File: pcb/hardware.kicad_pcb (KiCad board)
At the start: 2 copper layers, 16 parts, among them J1 Micro_SD_Card_Det_Hirose_DM3AT, U1 AS4C512M16D3L-12BIN, U2 A33, U3 TPS62095RGTR

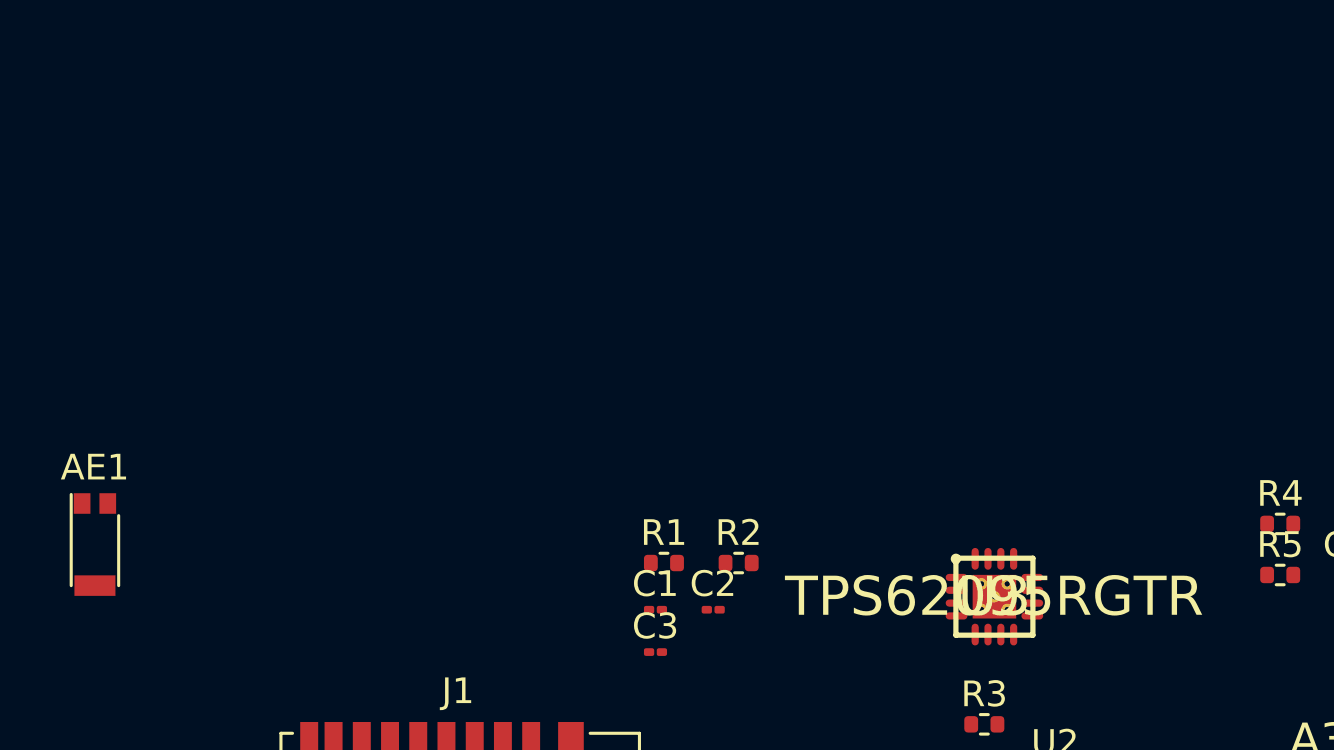
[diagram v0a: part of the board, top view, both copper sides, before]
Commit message: Added the 2.5V LDO
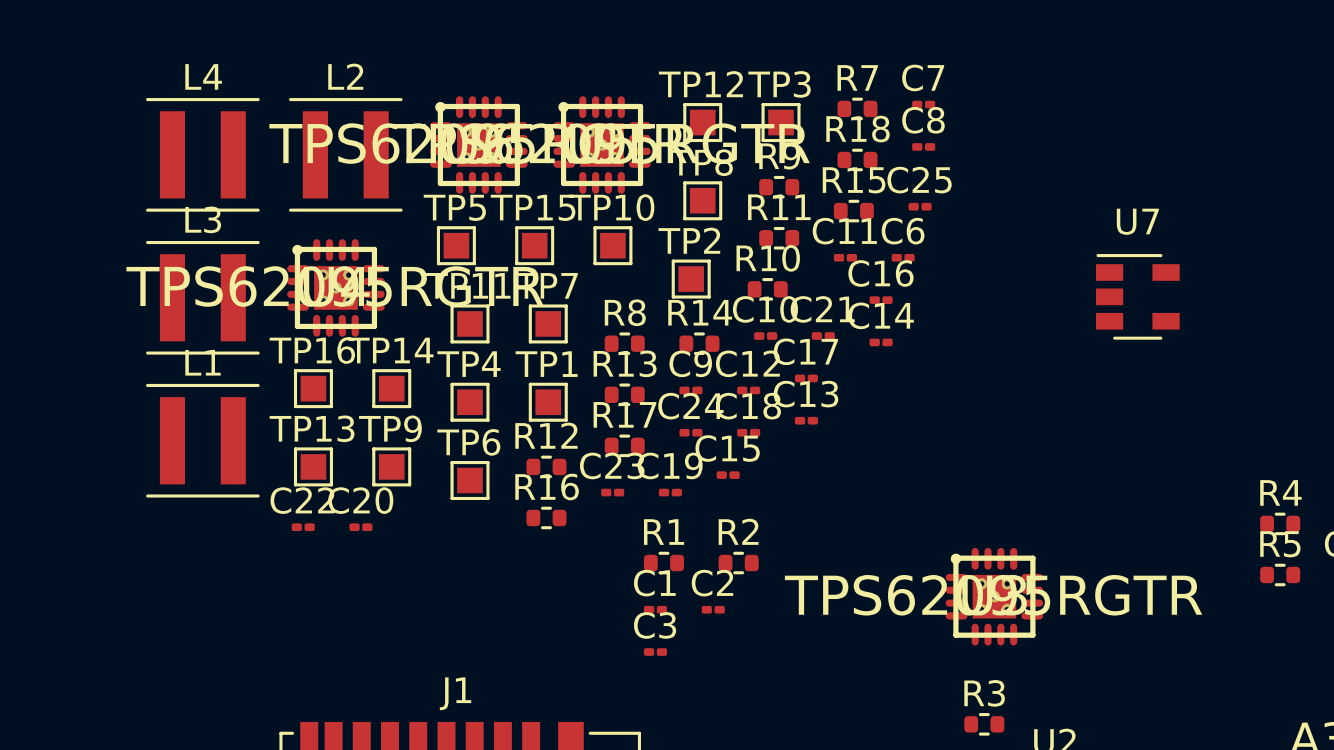
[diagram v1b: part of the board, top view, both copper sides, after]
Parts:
- removed AE1: Antenna, RF_Antenna:Pulse_W3011
- added C10: 22uF, Capacitor_SMD:C_01005_0402Metric, F.Cu at (120.1, 78.7)
- added C11: 22uF, Capacitor_SMD:C_01005_0402Metric, F.Cu at (123.2, 75.7)
- added C12: 10nF, Capacitor_SMD:C_01005_0402Metric, F.Cu at (119.5, 80.9)
- added C13: 450pF, Capacitor_SMD:C_01005_0402Metric, F.Cu at (121.7, 82.0)
- added C14: 22uF, Capacitor_SMD:C_01005_0402Metric, F.Cu at (124.6, 79.0)
- added C15: 22uF, Capacitor_SMD:C_01005_0402Metric, F.Cu at (118.7, 84.2)
- added C16: 22uF, Capacitor_SMD:C_01005_0402Metric, F.Cu at (124.6, 77.3)
- added C17: 22uF, Capacitor_SMD:C_01005_0402Metric, F.Cu at (121.7, 80.4)
- added C18: 10nF, Capacitor_SMD:C_01005_0402Metric, F.Cu at (119.5, 82.5)
- added C19: 5nF, Capacitor_SMD:C_01005_0402Metric, F.Cu at (116.4, 84.8)
- added C20: 10nF, Capacitor_SMD:C_01005_0402Metric, F.Cu at (104.3, 86.2)
- added C21: 5nF, Capacitor_SMD:C_01005_0402Metric, F.Cu at (122.4, 78.7)
- added C22: 22uF, Capacitor_SMD:C_01005_0402Metric, F.Cu at (102.1, 86.2)
- added C23: 22uF, Capacitor_SMD:C_01005_0402Metric, F.Cu at (114.2, 84.8)
- added C24: 22uF, Capacitor_SMD:C_01005_0402Metric, F.Cu at (117.2, 82.5)
- added C25: 22uF, Capacitor_SMD:C_01005_0402Metric, F.Cu at (126.1, 73.7)
- added C6: 22uF, Capacitor_SMD:C_01005_0402Metric, F.Cu at (125.5, 75.7)
- added C7: 10nF, Capacitor_SMD:C_01005_0402Metric, F.Cu at (126.3, 69.7)
- added C8: 450pF, Capacitor_SMD:C_01005_0402Metric, F.Cu at (126.3, 71.4)
- added C9: 22uF, Capacitor_SMD:C_01005_0402Metric, F.Cu at (117.2, 80.9)
- added L1: 1uH, Inductor_SMD:L_Coilcraft_XxL4020, F.Cu at (98.2, 82.8)
- added L2: 1uH, Inductor_SMD:L_Coilcraft_XxL4020, F.Cu at (103.8, 71.7)
- added L3: 1uH, Inductor_SMD:L_Coilcraft_XxL4020, F.Cu at (98.2, 77.3)
- added L4: 1uH, Inductor_SMD:L_Coilcraft_XxL4020, F.Cu at (98.2, 71.7)
- added R10: 120k, Resistor_SMD:R_0402_1005Metric, F.Cu at (120.2, 76.9)
- added R11: 110k, Resistor_SMD:R_0402_1005Metric, F.Cu at (120.6, 74.9)
- added R12: 160k, Resistor_SMD:R_0402_1005Metric, F.Cu at (111.6, 83.8)
- added R13: 82k, Resistor_SMD:R_0402_1005Metric, F.Cu at (114.6, 81.0)
- added R14: 220k, Resistor_SMD:R_0402_1005Metric, F.Cu at (117.5, 79.0)
- added R15: 0R, Resistor_SMD:R_0402_1005Metric, F.Cu at (123.6, 73.9)
- added R16: 0R, Resistor_SMD:R_0402_1005Metric, F.Cu at (111.6, 85.8)
- added R17: 0R, Resistor_SMD:R_0402_1005Metric, F.Cu at (114.6, 83.0)
- added R18: 0R, Resistor_SMD:R_0402_1005Metric, F.Cu at (123.7, 71.9)
- added R7: 470k, Resistor_SMD:R_0402_1005Metric, F.Cu at (123.7, 69.9)
- added R8: 150k, Resistor_SMD:R_0402_1005Metric, F.Cu at (114.6, 79.0)
- added R9: 330k, Resistor_SMD:R_0402_1005Metric, F.Cu at (120.6, 72.9)
- added TP1: TestPoint, TestPoint:TestPoint_Pad_1.0x1.0mm, F.Cu at (111.6, 81.3)
- added TP10: TestPoint, TestPoint:TestPoint_Pad_1.0x1.0mm, F.Cu at (114.2, 75.2)
- added TP11: TestPoint, TestPoint:TestPoint_Pad_1.0x1.0mm, F.Cu at (108.6, 78.3)
- added TP12: TestPoint, TestPoint:TestPoint_Pad_1.0x1.0mm, F.Cu at (117.7, 70.4)
- added TP13: TestPoint, TestPoint:TestPoint_Pad_1.0x1.0mm, F.Cu at (102.5, 83.8)
- added TP14: TestPoint, TestPoint:TestPoint_Pad_1.0x1.0mm, F.Cu at (105.5, 80.8)
- added TP15: TestPoint, TestPoint:TestPoint_Pad_1.0x1.0mm, F.Cu at (111.1, 75.2)
- added TP16: TestPoint, TestPoint:TestPoint_Pad_1.0x1.0mm, F.Cu at (102.5, 80.8)
- added TP2: TestPoint, TestPoint:TestPoint_Pad_1.0x1.0mm, F.Cu at (117.2, 76.5)
- added TP3: TestPoint, TestPoint:TestPoint_Pad_1.0x1.0mm, F.Cu at (120.7, 70.4)
- added TP4: TestPoint, TestPoint:TestPoint_Pad_1.0x1.0mm, F.Cu at (108.6, 81.3)
- added TP5: TestPoint, TestPoint:TestPoint_Pad_1.0x1.0mm, F.Cu at (108.1, 75.2)
- added TP6: TestPoint, TestPoint:TestPoint_Pad_1.0x1.0mm, F.Cu at (108.6, 84.4)
- added TP7: TestPoint, TestPoint:TestPoint_Pad_1.0x1.0mm, F.Cu at (111.6, 78.3)
- added TP8: TestPoint, TestPoint:TestPoint_Pad_1.0x1.0mm, F.Cu at (117.7, 73.5)
- added TP9: TestPoint, TestPoint:TestPoint_Pad_1.0x1.0mm, F.Cu at (105.5, 83.8)
- added U4: TPS62095RGTR, TI:TI_RTE_S-PWQFN-N16, F.Cu at (103.4, 76.9)
- added U5: TPS62095RGTR, TI:TI_RTE_S-PWQFN-N16, F.Cu at (113.7, 71.3)
- added U6: TPS62095RGTR, TI:TI_RTE_S-PWQFN-N16, F.Cu at (108.9, 71.3)
- added U7: AP131-25, Package_TO_SOT_SMD:SOT-23-5, F.Cu at (134.6, 77.2)
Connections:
- U2 pad K1: Net-(U2-PadK1) -> /ram/!LDQS
- U2 pad K2: Net-(U2-PadK2) -> /ram/LDQS
- U2 pad L12: +3V0 -> +3V3
- U2 pad N2: Net-(U2-PadN2) -> /ram/LDM
- U2 pad R1: Net-(U2-PadR1) -> /ram/!UDQS
- U2 pad T1: Net-(U2-PadT1) -> /ram/UDQS
- U2 pad T3: Net-(U2-PadT3) -> /ram/UDM
- U3 pad 1: Net-(U3-Pad1) -> Net-(L1-Pad1)
- U3 pad 10: Net-(U3-Pad10) -> +5V
- U3 pad 11: Net-(U3-Pad11) -> +5V
- U3 pad 12: Net-(U3-Pad12) -> +5V
- U3 pad 13: Net-(U3-Pad13) -> +5V
- U3 pad 14: Net-(U3-Pad14) -> GND
- U3 pad 15: Net-(U3-Pad15) -> GND
- U3 pad 17: Net-(U3-Pad17) -> GND
- U3 pad 2: Net-(U3-Pad2) -> Net-(L1-Pad1)
- U3 pad 3: Net-(U3-Pad3) -> +5V
- U3 pad 6: Net-(U3-Pad6) -> GND

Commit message: Random unknown commit
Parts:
- added C26: 10uF, Capacitor_SMD:C_01005_0402Metric, F.Cu at (179.1, 47.0)
- added C27: 0.1uF, Capacitor_SMD:C_01005_0402Metric, F.Cu at (182.3, 43.9)
- added C28: 10uF, Capacitor_SMD:C_01005_0402Metric, F.Cu at (181.3, 47.0)
- added R19: 0R, Resistor_SMD:R_0402_1005Metric, F.Cu at (176.5, 47.2)
- added R20: 100k, Resistor_SMD:R_0402_1005Metric, F.Cu at (148.2, 84.8)
- added R21: 100k, Resistor_SMD:R_0402_1005Metric, F.Cu at (151.1, 84.8)
- added R22: 10k, Resistor_SMD:R_0402_1005Metric, F.Cu at (154.0, 84.8)
- added R23: 100k, Resistor_SMD:R_0402_1005Metric, F.Cu at (148.2, 86.7)
- added R24: 100k, Resistor_SMD:R_0402_1005Metric, F.Cu at (151.1, 86.7)
- added R25: 100k, Resistor_SMD:R_0402_1005Metric, F.Cu at (148.2, 88.7)
- added TP17: TestPoint, TestPoint:TestPoint_Pad_1.0x1.0mm, F.Cu at (176.6, 44.6)
- added TP18: TestPoint, TestPoint:TestPoint_Pad_1.0x1.0mm, F.Cu at (179.6, 44.6)
- moved R4 52.6 mm to (88.1, 93.7)
- moved R5 52.6 mm to (88.1, 95.7)
- moved R6 52.6 mm to (91.0, 93.7)
- moved C4 52.6 mm to (90.7, 95.5)
- moved C5 52.6 mm to (92.9, 95.5)
- moved U3 49.6 mm to (79.5, 91.4)
- moved R3 49.6 mm to (79.1, 96.4)
- moved J1 32.5 mm to (135.9, 85.1), turned to 180 degrees
- moved C10 25.5 mm to (94.7, 76.2)
- moved C11 25.5 mm to (97.8, 73.2)
- moved C12 25.5 mm to (94.1, 78.3)
- moved C13 25.5 mm to (96.3, 79.5)
- moved C14 25.5 mm to (99.2, 76.5)
- moved C15 25.5 mm to (93.3, 81.6)
- moved C16 25.5 mm to (99.2, 74.8)
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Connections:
- J1 pad 1: Net-(J1-Pad1) -> /gpio/SD_DAT2
- J1 pad 10: Net-(J1-Pad10) -> /gpio/SD_DET
- J1 pad 11: Net-(J1-Pad11) -> GND
- J1 pad 2: Net-(J1-Pad2) -> /gpio/SD_DAT3
- J1 pad 3: Net-(J1-Pad3) -> /gpio/SD_CMD
- J1 pad 4: Net-(J1-Pad4) -> +3V3
- J1 pad 5: Net-(J1-Pad5) -> /gpio/SD_CLK
- J1 pad 6: Net-(J1-Pad6) -> GND
- J1 pad 7: Net-(J1-Pad7) -> /gpio/SD_DAT0
- J1 pad 8: Net-(J1-Pad8) -> /gpio/SD_DAT1
- J1 pad 9: Net-(J1-Pad9) -> GND
- U2 pad C7: Net-(U2-PadC7) -> /gpio/SD_DAT2
- U2 pad C8: Net-(U2-PadC8) -> /gpio/SD_CMD
- U2 pad C9: Net-(U2-PadC9) -> /gpio/SD_DAT0
- U2 pad D7: Net-(U2-PadD7) -> /gpio/SD_DAT3
- U2 pad D8: Net-(U2-PadD8) -> /gpio/SD_CLK
- U2 pad D9: Net-(U2-PadD9) -> /gpio/SD_DAT1
- U2 pad G14: Net-(U2-PadG14) -> /gpio/SD_DET
- U7 pad 1: Net-(U7-Pad1) -> +3V3
- U7 pad 2: Net-(U7-Pad2) -> GND
- U7 pad 3: Net-(U7-Pad3) -> +3V3

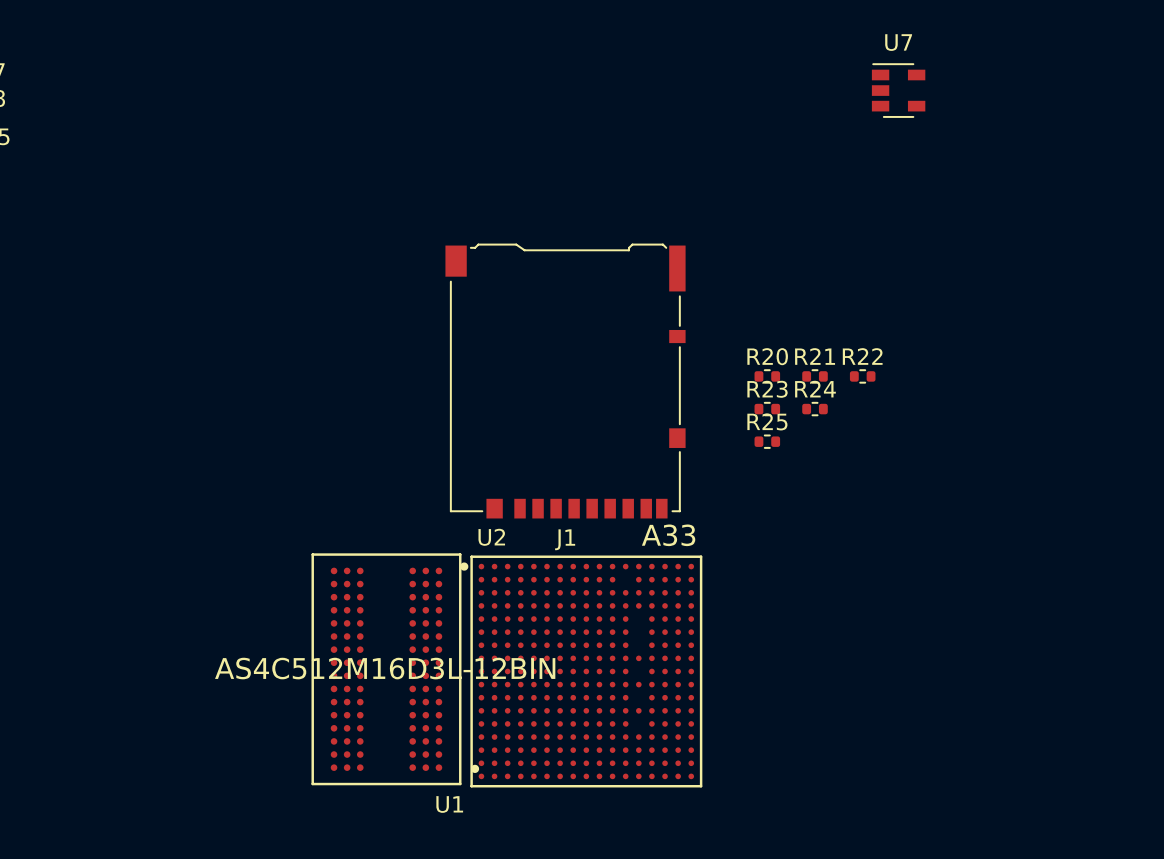
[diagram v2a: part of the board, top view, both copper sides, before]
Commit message: Just dropped all the parts on the board.
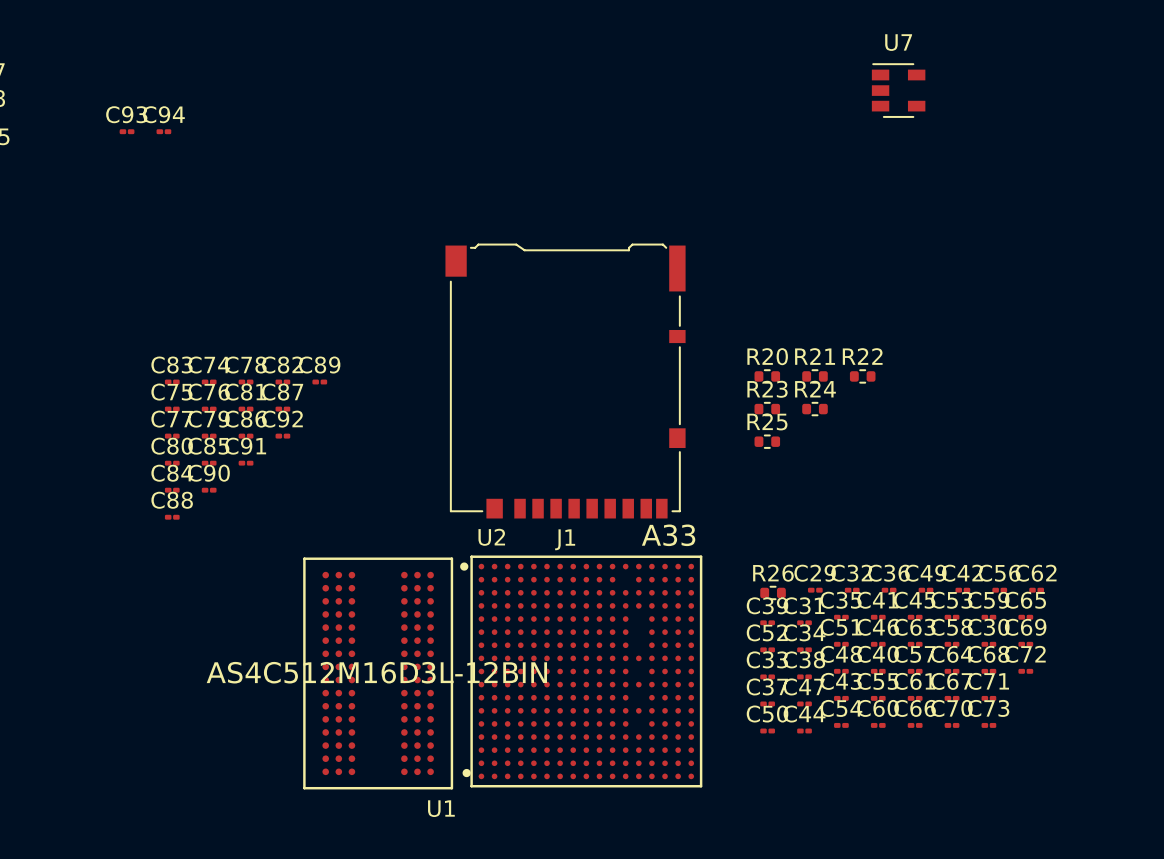
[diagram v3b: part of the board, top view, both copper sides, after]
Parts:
- added C29: 10uF, Capacitor_SMD:C_01005_0402Metric, F.Cu at (151.1, 97.8)
- added C30: 100nF, Capacitor_SMD:C_01005_0402Metric, F.Cu at (161.7, 101.1)
- added C31: 100nF, Capacitor_SMD:C_01005_0402Metric, F.Cu at (150.5, 99.8)
- added C32: 100nF, Capacitor_SMD:C_01005_0402Metric, F.Cu at (153.4, 97.8)
- added C33: 100nF, Capacitor_SMD:C_01005_0402Metric, F.Cu at (148.2, 103.1)
- added C34: 100nF, Capacitor_SMD:C_01005_0402Metric, F.Cu at (150.5, 101.4)
- added C35: 100nF, Capacitor_SMD:C_01005_0402Metric, F.Cu at (152.7, 99.4)
- added C36: 100nF, Capacitor_SMD:C_01005_0402Metric, F.Cu at (155.6, 97.8)
- added C37: 100nF, Capacitor_SMD:C_01005_0402Metric, F.Cu at (148.2, 104.7)
- added C38: 100nF, Capacitor_SMD:C_01005_0402Metric, F.Cu at (150.5, 103.1)
- added C39: 100nF, Capacitor_SMD:C_01005_0402Metric, F.Cu at (148.2, 99.8)
- added C40: 100nF, Capacitor_SMD:C_01005_0402Metric, F.Cu at (155.0, 102.7)
- added C41: 100nF, Capacitor_SMD:C_01005_0402Metric, F.Cu at (155.0, 99.4)
- added C42: 100nF, Capacitor_SMD:C_01005_0402Metric, F.Cu at (160.1, 97.8)
- added C43: 100nF, Capacitor_SMD:C_01005_0402Metric, F.Cu at (152.7, 104.4)
- added C44: 100nF, Capacitor_SMD:C_01005_0402Metric, F.Cu at (150.5, 106.4)
- added C45: 100nF, Capacitor_SMD:C_01005_0402Metric, F.Cu at (157.2, 99.4)
- added C46: 100nF, Capacitor_SMD:C_01005_0402Metric, F.Cu at (155.0, 101.1)
- added C47: 100nF, Capacitor_SMD:C_01005_0402Metric, F.Cu at (150.5, 104.7)
- added C48: 100nF, Capacitor_SMD:C_01005_0402Metric, F.Cu at (152.7, 102.7)
- added C49: 100nF, Capacitor_SMD:C_01005_0402Metric, F.Cu at (157.9, 97.8)
- added C50: 100nF, Capacitor_SMD:C_01005_0402Metric, F.Cu at (148.2, 106.4)
- added C51: 100nF, Capacitor_SMD:C_01005_0402Metric, F.Cu at (152.7, 101.1)
- added C52: 100nF, Capacitor_SMD:C_01005_0402Metric, F.Cu at (148.2, 101.4)
- added C53: 22uF, Capacitor_SMD:C_01005_0402Metric, F.Cu at (159.5, 99.4)
- added C54: 22uF, Capacitor_SMD:C_01005_0402Metric, F.Cu at (152.7, 106.0)
- added C55: 100nF, Capacitor_SMD:C_01005_0402Metric, F.Cu at (155.0, 104.4)
- added C56: 100nF, Capacitor_SMD:C_01005_0402Metric, F.Cu at (162.4, 97.8)
- added C57: 22uF, Capacitor_SMD:C_01005_0402Metric, F.Cu at (157.2, 102.7)
- added C58: 22uF, Capacitor_SMD:C_01005_0402Metric, F.Cu at (159.5, 101.1)
- added C59: 100nF, Capacitor_SMD:C_01005_0402Metric, F.Cu at (161.7, 99.4)
- added C60: 100nF, Capacitor_SMD:C_01005_0402Metric, F.Cu at (155.0, 106.0)
- added C61: 100nF, Capacitor_SMD:C_01005_0402Metric, F.Cu at (157.2, 104.4)
- added C62: 100nF, Capacitor_SMD:C_01005_0402Metric, F.Cu at (164.6, 97.8)
- added C63: 100nF, Capacitor_SMD:C_01005_0402Metric, F.Cu at (157.2, 101.1)
- added C64: 100nF, Capacitor_SMD:C_01005_0402Metric, F.Cu at (159.5, 102.7)
- added C65: 100nF, Capacitor_SMD:C_01005_0402Metric, F.Cu at (164.0, 99.4)
- added C66: 100nF, Capacitor_SMD:C_01005_0402Metric, F.Cu at (157.2, 106.0)
- added C67: 100nF, Capacitor_SMD:C_01005_0402Metric, F.Cu at (159.5, 104.4)
- added C68: 100nF, Capacitor_SMD:C_01005_0402Metric, F.Cu at (161.7, 102.7)
- added C69: 100nF, Capacitor_SMD:C_01005_0402Metric, F.Cu at (164.0, 101.1)
- added C70: 100nF, Capacitor_SMD:C_01005_0402Metric, F.Cu at (159.5, 106.0)
- added C71: 22uF, Capacitor_SMD:C_01005_0402Metric, F.Cu at (161.7, 104.4)
- added C72: 22uF, Capacitor_SMD:C_01005_0402Metric, F.Cu at (164.0, 102.7)
- added C73: 100nF, Capacitor_SMD:C_01005_0402Metric, F.Cu at (161.7, 106.0)
- added C74: 100nF, Capacitor_SMD:C_01005_0402Metric, F.Cu at (114.2, 85.1)
- added C75: 100nF, Capacitor_SMD:C_01005_0402Metric, F.Cu at (111.9, 86.7)
- added C76: 100nF, Capacitor_SMD:C_01005_0402Metric, F.Cu at (114.2, 86.7)
- added C77: 100nF, Capacitor_SMD:C_01005_0402Metric, F.Cu at (111.9, 88.4)
- added C78: 100nF, Capacitor_SMD:C_01005_0402Metric, F.Cu at (116.4, 85.1)
- added C79: 100nF, Capacitor_SMD:C_01005_0402Metric, F.Cu at (114.2, 88.4)
- added C80: 100nF, Capacitor_SMD:C_01005_0402Metric, F.Cu at (111.9, 90.0)
- added C81: 100nF, Capacitor_SMD:C_01005_0402Metric, F.Cu at (116.4, 86.7)
- added C82: 100nF, Capacitor_SMD:C_01005_0402Metric, F.Cu at (118.7, 85.1)
- added C83: 100nF, Capacitor_SMD:C_01005_0402Metric, F.Cu at (111.9, 85.1)
- added C84: 100nF, Capacitor_SMD:C_01005_0402Metric, F.Cu at (111.9, 91.7)
- added C85: 100nF, Capacitor_SMD:C_01005_0402Metric, F.Cu at (114.2, 90.0)
- added C86: 100nF, Capacitor_SMD:C_01005_0402Metric, F.Cu at (116.4, 88.4)
- added C87: 100nF, Capacitor_SMD:C_01005_0402Metric, F.Cu at (118.7, 86.7)
- added C88: 100nF, Capacitor_SMD:C_01005_0402Metric, F.Cu at (111.9, 93.3)
- added C89: 100nF, Capacitor_SMD:C_01005_0402Metric, F.Cu at (120.9, 85.1)
- added C90: 100nF, Capacitor_SMD:C_01005_0402Metric, F.Cu at (114.2, 91.7)
- added C91: 100nF, Capacitor_SMD:C_01005_0402Metric, F.Cu at (116.4, 90.0)
- added C92: 100nF, Capacitor_SMD:C_01005_0402Metric, F.Cu at (118.7, 88.4)
- added C93: 100nF, Capacitor_SMD:C_01005_0402Metric, F.Cu at (109.1, 69.8)
- added C94: 22uF, Capacitor_SMD:C_01005_0402Metric, F.Cu at (111.4, 69.8)
- added R26: 0R, Resistor_SMD:R_0402_1005Metric, F.Cu at (148.6, 98.0)
- moved U1 0.57 mm to (124.5, 102.9)
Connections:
- U2 pad H17: Net-(U2-PadH17) -> /HPVCCBP
- U2 pad K13: Net-(U2-PadK13) -> +3V0
- U2 pad M8: Net-(U2-PadM8) -> /VCC-EFUSE
